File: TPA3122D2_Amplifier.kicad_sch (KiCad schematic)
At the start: 49 parts, among them J1 Barrel_Jack_Switch, J2 Screw_Terminal_01x02, J3 AudioJack3, J4 Screw_Terminal_01x04, Q1 TSM480P06, SW1 SW_Push_SPDT, U1 TPA3122D2

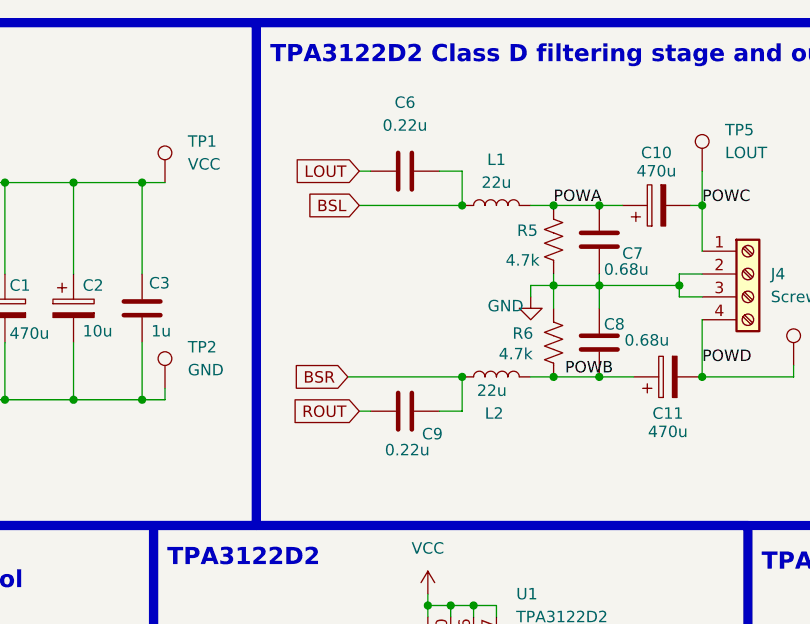
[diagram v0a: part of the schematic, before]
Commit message: fixed misplaced capacitors C6 & C9
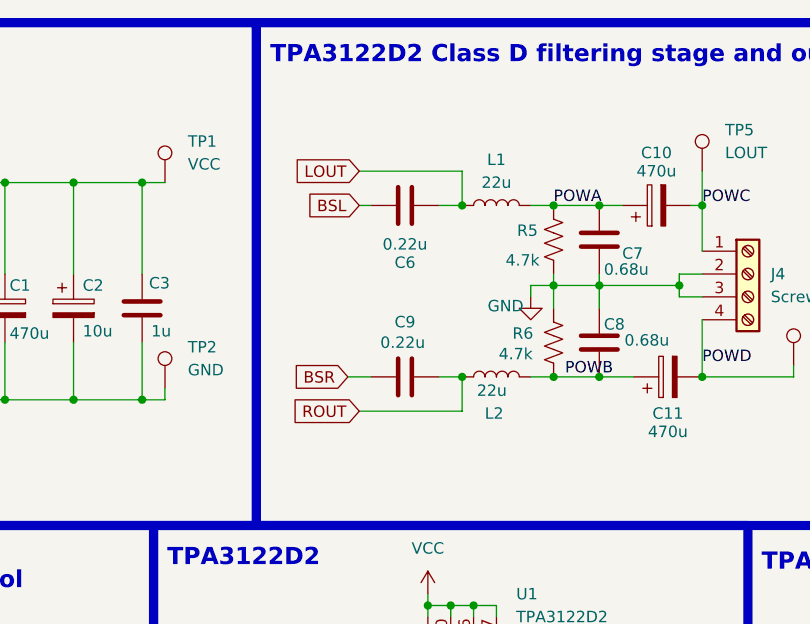
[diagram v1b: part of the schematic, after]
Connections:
- net BSL: now also C6.2; no longer C6.1, L1.1
- net BSR: now also C9.2; no longer C9.1, L2.1
- net LOUT: now also C6.1, L1.1; no longer C6.2
- net ROUT: now also C9.1, L2.1; no longer C9.2
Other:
- moved on the sheet: C6, C9
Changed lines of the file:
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@@
+	)
+	(junction
+		(at 156.21 62.23)
+		(diameter 0)
+		(color 0 0 0 0)
+	)
+	(junction
+		(at 57.15 62.23)
+		(diameter 0)
+		(color 0 0 0 0)
+	)
+	(junction
+		(at 57.15 64.77)
+		(diameter 0)
+		(color 0 0 0 0)
+	)
+	(junction
+		(at 127 118.11)
+		(diameter 0)
+		(color 0 0 0 0)
+	)
+	(junction
+		(at 190.5 110.49)
+		(diameter 0)
+		(color 0 0 0 0)
+	)
+	(junction
+		(at 104.14 115.57)
+		(diameter 0)
+		(color 0 0 0 0)
+	)
+	(junction
+		(at 172.72 72.39)
+		(diameter 0)
+		(color 0 0 0 0)
 	)
 	(junction
@@
 	)
 	(junction
-		(at 156.21 62.23)
-		(diameter 0)
-		(color 0 0 0 0)
-	)
-	(junction
-		(at 57.15 62.23)
-		(diameter 0)
-		(color 0 0 0 0)
-	)
-	(junction
-		(at 57.15 64.77)
-		(diameter 0)
-		(color 0 0 0 0)
-	)
-	(junction
-		(at 127 118.11)
-		(diameter 0)
-		(color 0 0 0 0)
-	)
-	(junction
-		(at 190.5 110.49)
-		(diameter 0)
-		(color 0 0 0 0)
-	)
-	(junction
-		(at 104.14 115.57)
-		(diameter 0)
-		(color 0 0 0 0)
-	)
-	(junction
-		(at 172.72 72.39)
-		(diameter 0)
-		(color 0 0 0 0)
-	)
-	(junction
 		(at 55.88 50.8)
 		(diameter 0)
@@
 	)
 	(junction
+		(at 146.05 53.34)
+		(diameter 0)
+		(color 0 0 0 0)
+	)
+	(junction
 		(at 104.14 128.27)
 		(diameter 0)
@@
 		(color 0 0 0 0)
 	)
-	(junction
-		(at 146.05 53.34)
-		(diameter 0)
-		(color 0 0 0 0)
-	)
 	(no_connect
 		(at 67.31 45.72)
@@
 	(wire
 		(pts
-			(xy 143.51 76.2) (xy 146.05 76.2)
-		)
-		(stroke
-			(width 0)
-			(type default)
-		)
-	)
-	(wire
-		(pts
 			(xy 102.87 50.8) (xy 110.49 50.8)
 		)
@@
 	(wire
 		(pts
+			(xy 133.35 72.39) (xy 135.89 72.39)
+		)
+		(stroke
+			(width 0)
+			(type default)
+		)
+	)
+	(wire
+		(pts
 			(xy 46.99 105.41) (xy 46.99 106.68)
 		)
@@
 	(wire
 		(pts
+			(xy 134.62 53.34) (xy 135.89 53.34)
+		)
+		(stroke
+			(width 0)
+			(type default)
+		)
+	)
+	(wire
+		(pts
 			(xy 229.87 110.49) (xy 229.87 111.76)
 		)
@@
 	(wire
 		(pts
-			(xy 143.51 49.53) (xy 146.05 49.53)
-		)
-		(stroke
-			(width 0)
-			(type default)
-		)
-	)
-	(wire
-		(pts
 			(xy 127 107.95) (xy 129.54 107.95)
 		)
@@
 	(wire
 		(pts
+			(xy 146.05 72.39) (xy 146.05 76.2)
+		)
+		(stroke
+			(width 0)
+			(type default)
+		)
+	)
+	(wire
+		(pts
+			(xy 143.51 53.34) (xy 146.05 53.34)
+		)
+		(stroke
+			(width 0)
+			(type default)
+		)
+	)
+	(wire
+		(pts
 			(xy 110.49 74.93) (xy 113.03 74.93)
 		)
@@
 	(wire
 		(pts
-			(xy 134.62 53.34) (xy 146.05 53.34)
-		)
-		(stroke
-			(width 0)
-			(type default)
-		)
-	)
-	(wire
-		(pts
 			(xy 171.45 53.34) (xy 172.72 53.34)
 		)
@@
 	(wire
 		(pts
+			(xy 134.62 76.2) (xy 146.05 76.2)
+		)
+		(stroke
+			(width 0)
+			(type default)
+		)
+	)
+	(wire
+		(pts
 			(xy 87.63 50.8) (xy 95.25 50.8)
 		)
@@
 	(wire
 		(pts
-			(xy 133.35 72.39) (xy 146.05 72.39)
-		)
-		(stroke
-			(width 0)
-			(type default)
-		)
-	)
-	(wire
-		(pts
 			(xy 146.05 53.34) (xy 146.05 49.53)
 		)
@@
 	(wire
 		(pts
+			(xy 143.51 72.39) (xy 146.05 72.39)
+		)
+		(stroke
+			(width 0)
+			(type default)
+		)
+	)
+	(wire
+		(pts
 			(xy 210.82 110.49) (xy 210.82 111.76)
 		)
@@
 	(wire
 		(pts
-			(xy 134.62 49.53) (xy 135.89 49.53)
+			(xy 134.62 49.53) (xy 146.05 49.53)
 		)
 		(stroke
@@
 	(wire
 		(pts
-			(xy 134.62 76.2) (xy 135.89 76.2)
-		)
-		(stroke
-			(width 0)
-			(type default)
-		)
-	)
-	(wire
-		(pts
 			(xy 226.06 110.49) (xy 229.87 110.49)
 		)
@@
 		(pts
 			(xy 142.24 132.08) (xy 144.78 132.08)
-		)
-		(stroke
-			(width 0)
-			(type default)
-		)
-	)
-	(wire
-		(pts
-			(xy 146.05 72.39) (xy 146.05 76.2)
 		)
 		(stroke
@@
 	(symbol
 		(lib_id "Device:C")
-		(at 139.7 76.2 270)
+		(at 139.7 72.39 270)
 		(unit 1)
 		(exclude_from_sim no)
@@
 		(dnp no)
 		(property "Reference" "C9"
-			(at 142.748 78.74 90)
+			(at 139.7 66.294 90)
 			(effects
 				(font
@@
 		)
 		(property "Value" "0.22u"
-			(at 139.954 80.518 90)
+			(at 139.446 68.58 90)
 			(effects
 				(font
@@
 		)
 		(property "Footprint" "Capacitor_THT:C_Disc_D4.3mm_W1.9mm_P5.00mm"
-			(at 135.89 77.1652 0)
+			(at 135.89 73.3552 0)
 			(effects
 				(font
@@
 		)
 		(property "Datasheet" "~"
-			(at 139.7 76.2 0)
+			(at 139.7 72.39 0)
 			(effects
 				(font
@@
 		)
 		(property "Description" "Unpolarized capacitor"
-			(at 139.7 76.2 0)
+			(at 139.7 72.39 0)
 			(effects
 				(font
@@
 	(symbol
 		(lib_id "Device:C")
-		(at 139.7 49.53 270)
+		(at 139.7 53.34 270)
 		(unit 1)
 		(exclude_from_sim no)
@@
 		(on_board yes)
 		(dnp no)
-		(fields_autoplaced yes)
 		(property "Reference" "C6"
-			(at 139.7 41.91 90)
+			(at 139.7 59.69 90)
 			(effects
 				(font
@@
 		)
 		(property "Value" "0.22u"
-			(at 139.7 44.45 90)
+			(at 139.7 57.658 90)
 			(effects
 				(font
@@
 		)
 		(property "Footprint" "Capacitor_THT:C_Disc_D4.3mm_W1.9mm_P5.00mm"
-			(at 135.89 50.4952 0)
+			(at 135.89 54.3052 0)
 			(effects
 				(font
@@
 		)
 		(property "Datasheet" "~"
-			(at 139.7 49.53 0)
+			(at 139.7 53.34 0)
 			(effects
 				(font
@@
 		)
 		(property "Description" "Unpolarized capacitor"
-			(at 139.7 49.53 0)
-			(effects
-				(font
+			(at 139.7 53.34 0)
+			(effects
+				(font

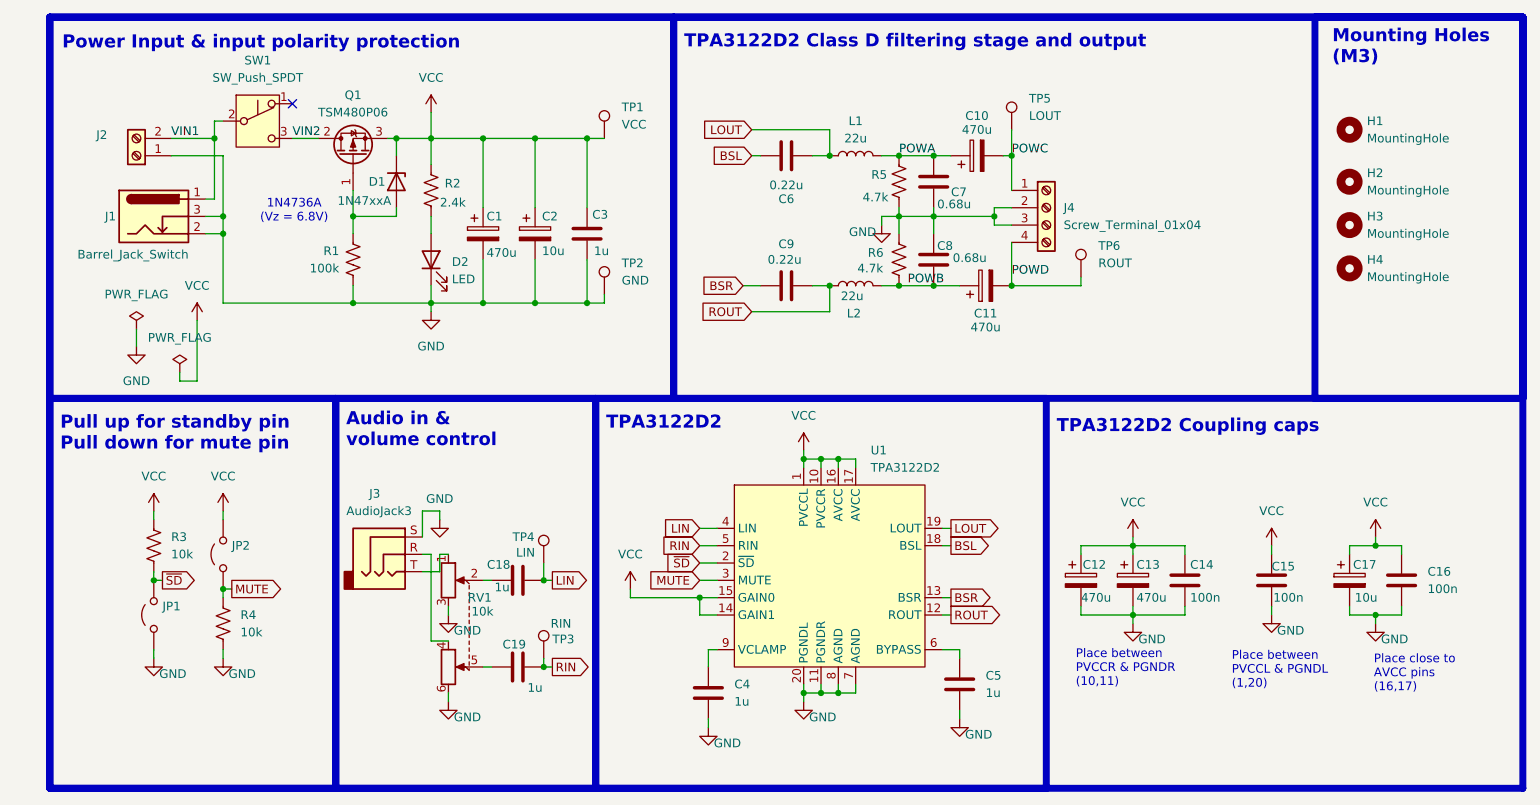
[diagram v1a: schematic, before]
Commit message: updated audio connector
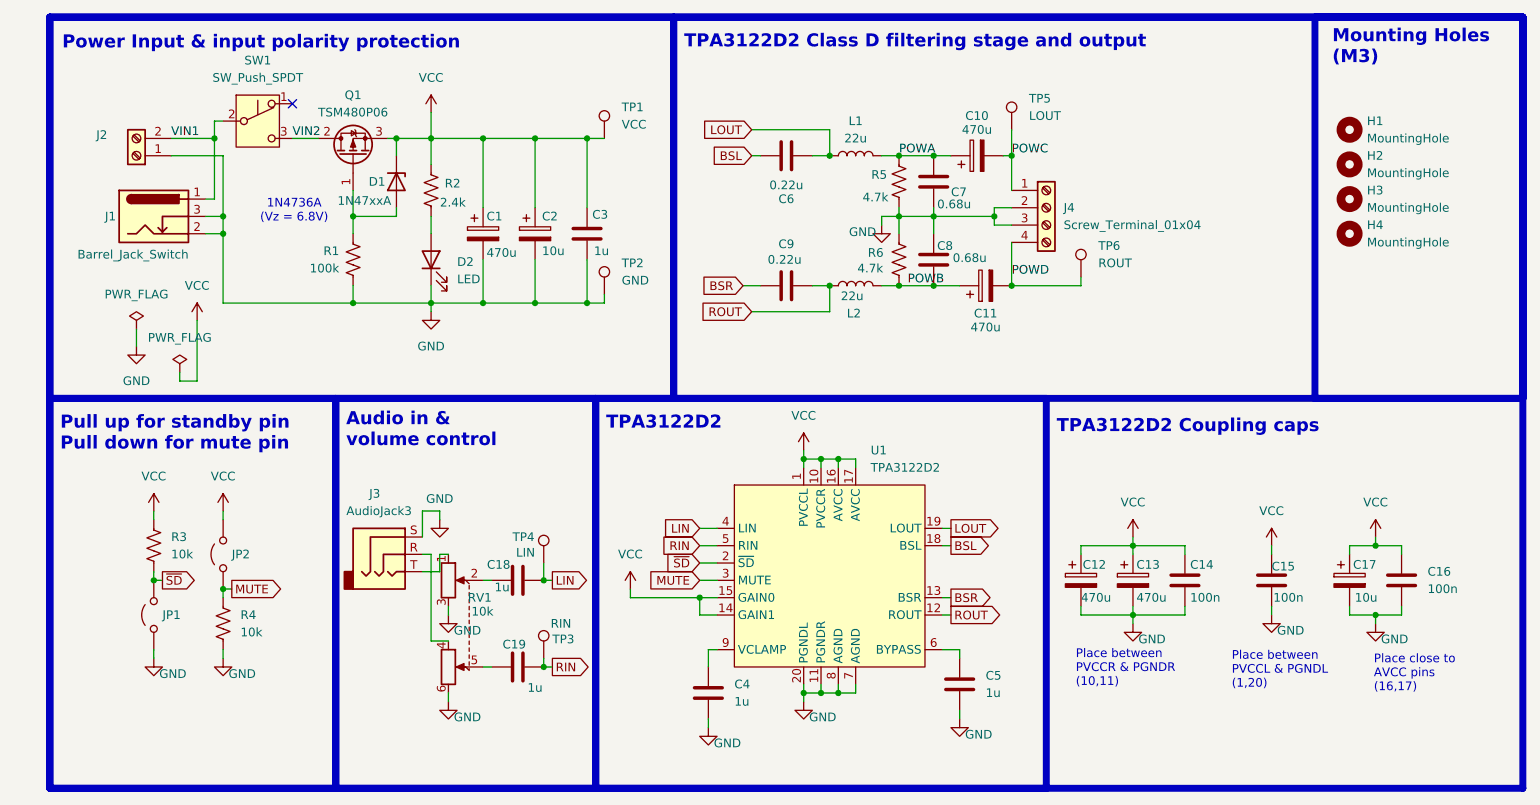
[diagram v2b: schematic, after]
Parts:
- J3: footprint Connector_Audio:Jack_3.5mm_CUI_SJ1-3533NG_Horizontal -> myparts:Jack_3.5mm_CUI_SJ1-3523N_Horizontal

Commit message: fixed terminal blocks
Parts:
- J2: footprint TerminalBlock:TerminalBlock_Altech_AK300-2_P5.00mm -> TerminalBlock_Phoenix:TerminalBlock_Phoenix_MKDS-1,5-2_1x02_P5.00mm_Horizontal
- J4: footprint TerminalBlock:TerminalBlock_Altech_AK300-4_P5.00mm -> TerminalBlock_Phoenix:TerminalBlock_Phoenix_MKDS-1,5-4_1x04_P5.00mm_Horizontal
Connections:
- net POWC: now also J4.4 (Pin_4); no longer J4.1 (Pin_1)
- net POWD: now also J4.1 (Pin_1); no longer J4.4 (Pin_4)
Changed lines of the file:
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@@
 	(symbol
 		(lib_id "Connector:Screw_Terminal_01x04")
-		(at 177.8 60.96 0)
-		(unit 1)
-		(exclude_from_sim no)
-		(in_bom yes)
-		(on_board yes)
-		(dnp no)
-		(fields_autoplaced yes)
+		(at 177.8 63.5 0)
+		(mirror x)
+		(unit 1)
+		(exclude_from_sim no)
+		(in_bom yes)
+		(on_board yes)
+		(dnp no)
 		(property "Reference" "J4"
-			(at 180.34 60.9599 0)
+			(at 180.34 63.5001 0)
 			(effects
 				(font
@@
 		)
 		(property "Value" "Screw_Terminal_01x04"
-			(at 180.34 63.4999 0)
-			(effects
-				(font
-					(size 1.27 1.27)
-				)
-				(justify left)
-			)
-		)
-		(property "Footprint" "TerminalBlock:TerminalBlock_Altech_AK300-4_P5.00mm"
-			(at 177.8 60.96 0)
+			(at 180.34 60.9601 0)
+			(effects
+				(font
+					(size 1.27 1.27)
+				)
+				(justify left)
+			)
+		)
+		(property "Footprint" "TerminalBlock_Phoenix:TerminalBlock_Phoenix_MKDS-1,5-4_1x04_P5.00mm_Horizontal"
+			(at 177.8 63.5 0)
 			(effects
 				(font
@@
 		)
 		(property "Datasheet" "~"
-			(at 177.8 60.96 0)
+			(at 177.8 63.5 0)
 			(effects
 				(font
@@
 		)
 		(property "Description" "Generic screw terminal, single row, 01x04, script generated (kicad-library-utils/schlib/autogen/connector/)"
-			(at 177.8 60.96 0)
+			(at 177.8 63.5 0)
 			(effects
 				(font
@@
 			)
 		)
-		(property "Footprint" "TerminalBlock:TerminalBlock_Altech_AK300-2_P5.00mm"
+		(property "Footprint" "TerminalBlock_Phoenix:TerminalBlock_Phoenix_MKDS-1,5-2_1x02_P5.00mm_Horizontal"
 			(at 44.45 53.34 0)
 			(effects
